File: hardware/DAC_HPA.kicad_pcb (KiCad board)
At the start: 4 copper layers, 100 x 80 mm, 537 parts, among them J101 GCT USB4105-GF-A, J201 PCB pads (no component), J202 PCB pads (no component), J701 G-Switch GT-3321667P-01, J702 HRO PJ-332A-6A, J703 1 × 6, K601 TLP3545A, K602 TLP3545A, K603 TLP3545A, K604 TLP3545A, Q207 AO3400A, Q502 AO3400A, Q503 AO3400A, Q504 AO3400A, Q505 AO3400A, Q506 AO3400A, Q507 MMBT3904, Q612 MMBT3904, Q614 MMBT3904, Q616 AO3400A, Q617 AO3400A, Q618 2N7002, Q619 AO3400A, Q620 AO3400A, Q621 2N7002, Q622 AO3400A, Q623 MMBT3904, Q624 MMBT3904, Q625 MMBT3904, Q626 MMBT3904, Q627 MMBT3904, U101 ST USBLC6-2SC6, U102 TI TPS25200DRVR, U103 TI TPD2E2U06DRLR, U201 CH32V307RCT6, U202 AGRV2KQ32, U205 74LVC1G157, U206 74LVC1G11, U208 74LVC3G34, U301 ES9018K2M, U302 3.3 V, 250 mA, U303 1.300 V (R533/R534), U401 OPA1622IDRCR, U402 OPA1622IDRCR, U403 OPA2210IDR, U404 OPA2210IDR, U501 +3.85 / -3.72 V, U502 3.3 V, 150 mA, U503 TI TPS259621DDAR, U504 3.3 V, 1 A, U505 TI TMUX1101DBVR, U603 TLV1704, U604 OPA2333, U605 TLV3402, U606 TLV1704, U607 74AUP1G17, U608 74LVC1G74, U609 TLV1704, U610 TLV1704, U611 TLV1704, U612 TLV1704, U613 TLV3402, U614 TLV3402, U615 TLV3402, U616 TLV3402, U617 TLV3402, U618 TLV3402, U619 TLV3402, U620 TLV3402, X201 80.000 MHz, X202 49.152 MHz, X203 45.1584 MHz, Y201 8 MHz

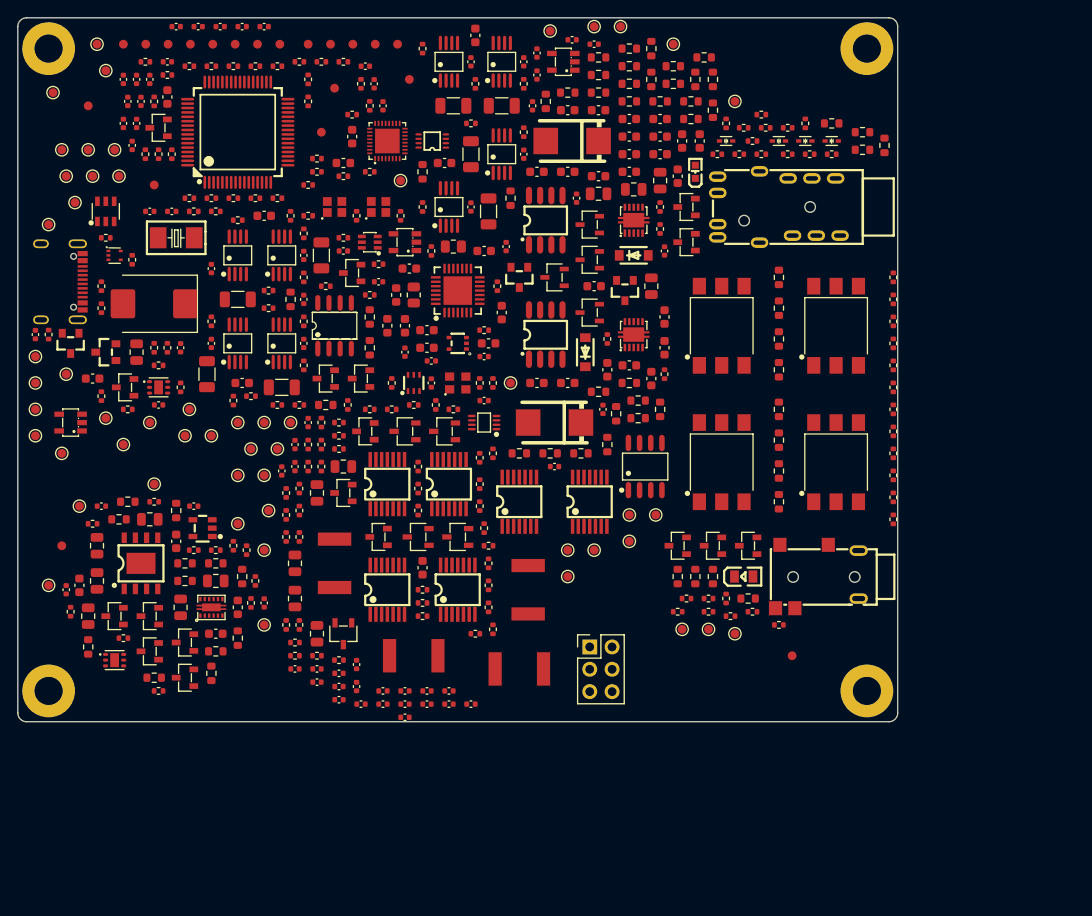
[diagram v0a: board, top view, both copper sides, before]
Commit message: Reassess DAC placement and add audio EMI geometry audit
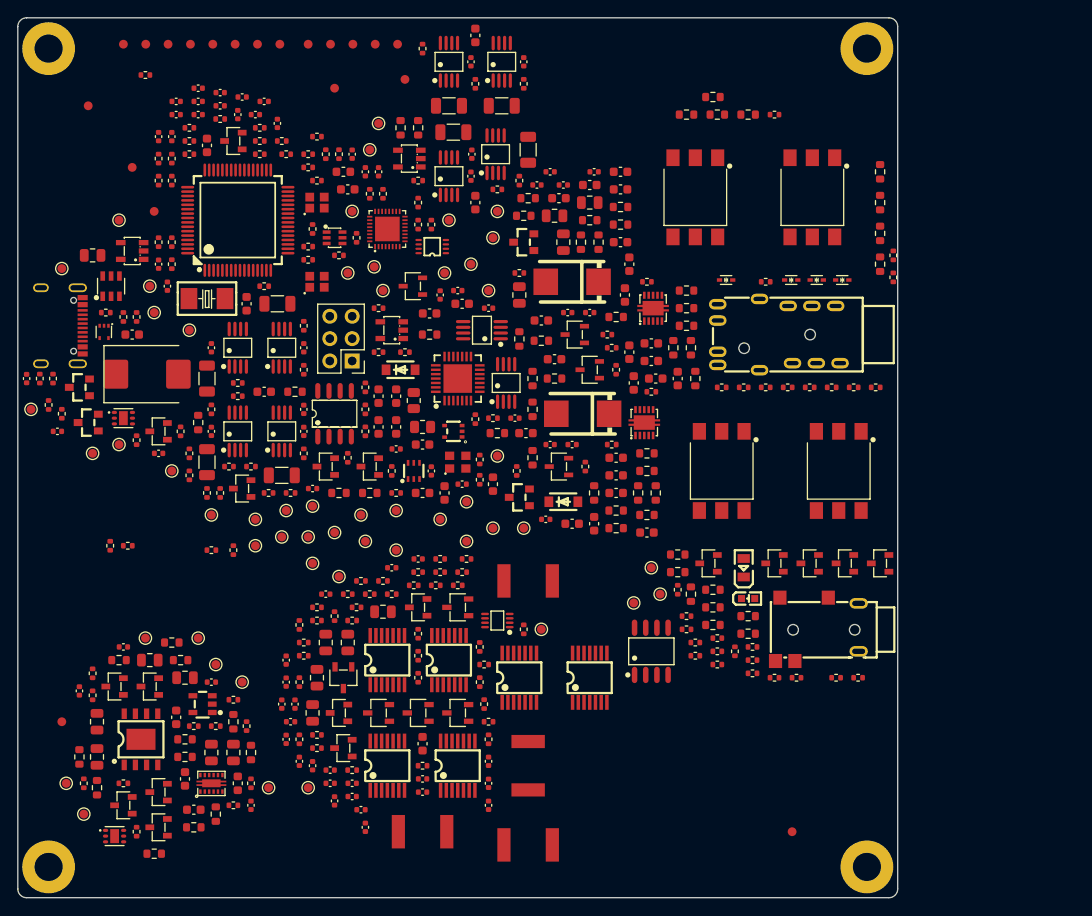
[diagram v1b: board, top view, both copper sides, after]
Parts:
- U403, U404: value OPA2210IDR -> OPA2210IDGKR; footprint JLC_Imported:SOIC-8_L4.9-W3.9-P1.27-LS6.0-BL-2 -> JLC_Imported:VSSOP-8_L3.0-W3.0-P0.65-LS5.0-BL
- moved R940 77.2 mm to (62.0, 100.5)
- moved R941 74.1 mm to (64.5, 100.5)
- moved TP738 69.0 mm to (45.5, 127.0)
- moved R950 64.1 mm to (128.5, 115.0)
- moved R951 61.8 mm to (117.0, 112.5), turned to 0 degrees
- moved R937 61.1 mm to (126.0, 115.0)
- moved R936 59.0 mm to (123.5, 114.5)
- moved R935 58.9 mm to (119.5, 113.5)
- moved R934 57.1 mm to (119.5, 112.0)
- moved TP708 56.9 mm to (88.0, 97.0)
- moved R702 56.5 mm to (121.5, 112.0), turned to 90 degrees
- moved C426 54.6 mm to (100.0, 97.0)
- moved R445 54.4 mm to (108.0, 98.0)
- moved R938 53.0 mm to (81.0, 78.0)
- moved R444 53.0 mm to (111.5, 96.5), turned to 0 degrees
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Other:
- board size 100 x 80 mm -> 100 x 100 mm

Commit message: Manually review 120x100 layout with JLCPCB rules and ESD escapes
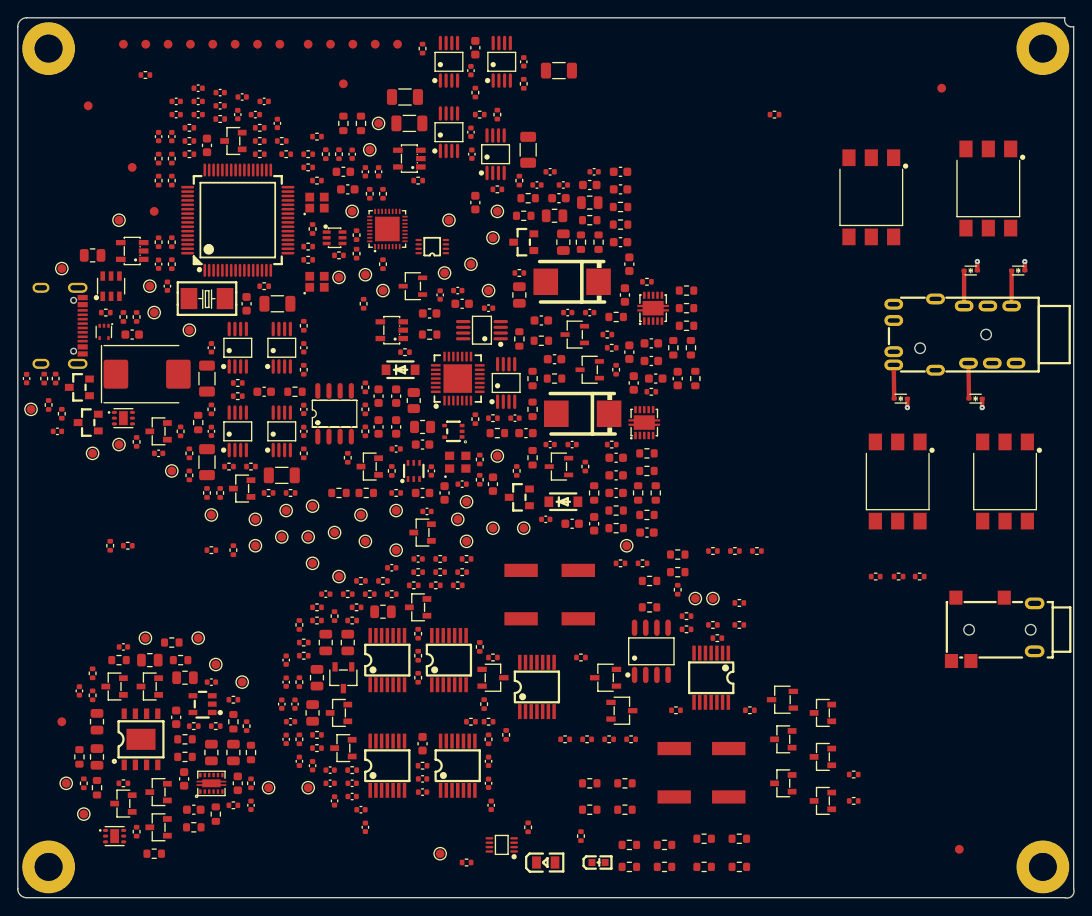
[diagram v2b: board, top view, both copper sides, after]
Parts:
- removed J703: 1 × 6, Connector_PinHeader_2.54mm:PinHeader_2x03_P2.54mm_Vertical
- moved R903 81.0 mm to (105.0, 130.0)
- moved R902 79.7 mm to (109.0, 130.0)
- moved R907 79.2 mm to (105.0, 127.0)
- moved R915 77.5 mm to (122.0, 133.3), turned to 0 degrees
- moved R906 76.3 mm to (109.0, 127.0)
- moved R914 75.0 mm to (118.0, 133.3), turned to 0 degrees
- moved R911 73.8 mm to (122.0, 136.5), turned to 0 degrees
- moved R910 71.4 mm to (118.0, 136.5), turned to 0 degrees
- moved FID4 69.0 mm to (145.0, 48.0)
- moved R916 47.3 mm to (102.2, 122.0)
- moved R918 46.0 mm to (107.2, 122.0)
- moved Q626 45.9 mm to (126.9, 117.5)
- moved R917 44.9 mm to (104.7, 122.0)
- moved R925 43.2 mm to (111.0, 102.0), turned to 0 degrees
- moved R919 42.0 mm to (109.7, 122.0)
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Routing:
- net GND: track 0.00 -> 4.08 mm, vias 0 -> 4
- net JACK_RP: track 0.00 -> 4.03 mm
- net JACK_RN: track 0.00 -> 4.03 mm
- net JACK_LN: track 0.00 -> 4.03 mm
- net JACK_LP: track 0.00 -> 3.83 mm
- added copper zone on In1.Cu, net GND
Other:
- board size 100 x 100 mm -> 120 x 100 mm
- board text added: "MANUAL LAYOUT REVIEW — PARTIAL ROUTE — NO FABRICATION OUTPUT"
- board text removed: "PROVISIONAL PLACEMENT — UNROUTED — NO FABRICATION OUTPUT"
